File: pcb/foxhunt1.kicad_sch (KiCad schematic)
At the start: 0 parts

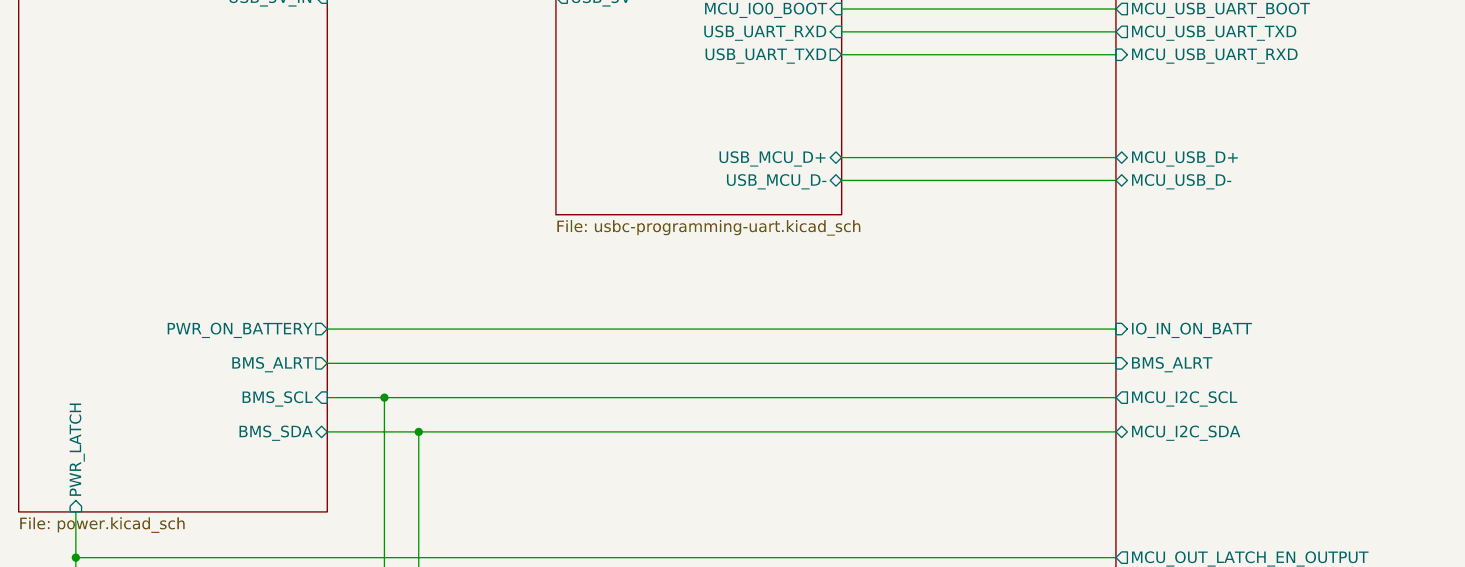
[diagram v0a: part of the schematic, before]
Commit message: Fix second mass-symbol-update reversion (recurred at same scale)
Same class of damage as the previous fix (commit 4ab9510) -- another
project-wide symbol resync reverted ~65 Datasheet fields and 5 Footprints
(Y2 crystal back to the wrong 5.0x3.2mm package again, U9/U12/U10/Y1
footprints back to non-stock equivalents) across all 7 schematic files.
Restored every field to its previously-verified value.

Also caught two real, independent bugs surfaced while re-checking (not
caused by this reversion, pre-existing): R32/R33/R43/R18 (10k YAGEO
RT0603BRD0710KL pull-ups, C95204) all had a mismatched Datasheet pointing
to a different resistor's PDF (RC0805FR-0710KL, wrong package family);
C36's Datasheet had drifted back to a different capacitor's PDF again
(same bug fixed once already this session).

ERC clean, same 14 pre-existing errors, no regressions.

Co-Authored-By: Claude Sonnet 5 <noreply@anthropic.com>
Claude-Session: https://claude.ai/code/session_01LhLkuH6sQ5GbUZ61bG7p2h
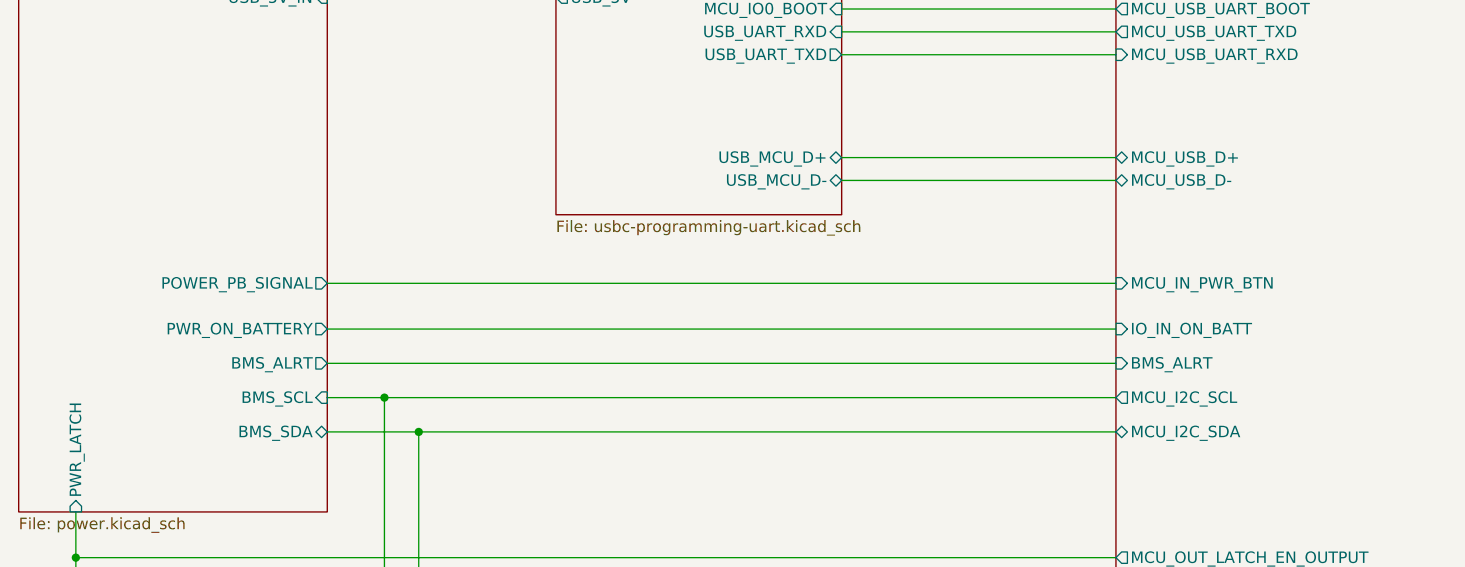
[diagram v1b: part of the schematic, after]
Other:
- sheet Power ports: added POWER_PB_SIGNAL; removed none
- sheet mcu-esp32 ports: added MCU_IN_PWR_BTN; removed none
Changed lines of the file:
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@@
+	(wire
+		(pts
+			(xy 78.74 74.93) (xy 166.37 74.93)
+		)
+		(stroke
+			(width 0)
+			(type default)
+		)
+	)
 	(wire
 		(pts
@@
 			)
 		)
+		(pin "POWER_PB_SIGNAL" output
+			(at 78.74 74.93 0)
+			(effects
+				(font
+					(size 1.27 1.27)
+				)
+				(justify right)
+			)
+		)
 		(instances
 			(project "foxhunt1"
@@
 			(effects
 				(font
+					(size 1.27 1.27)
+				)
+				(justify left)
+			)
+		)
+		(pin "MCU_IN_PWR_BTN" input
+			(at 166.37 74.93 180)
+			(effects
+				(font

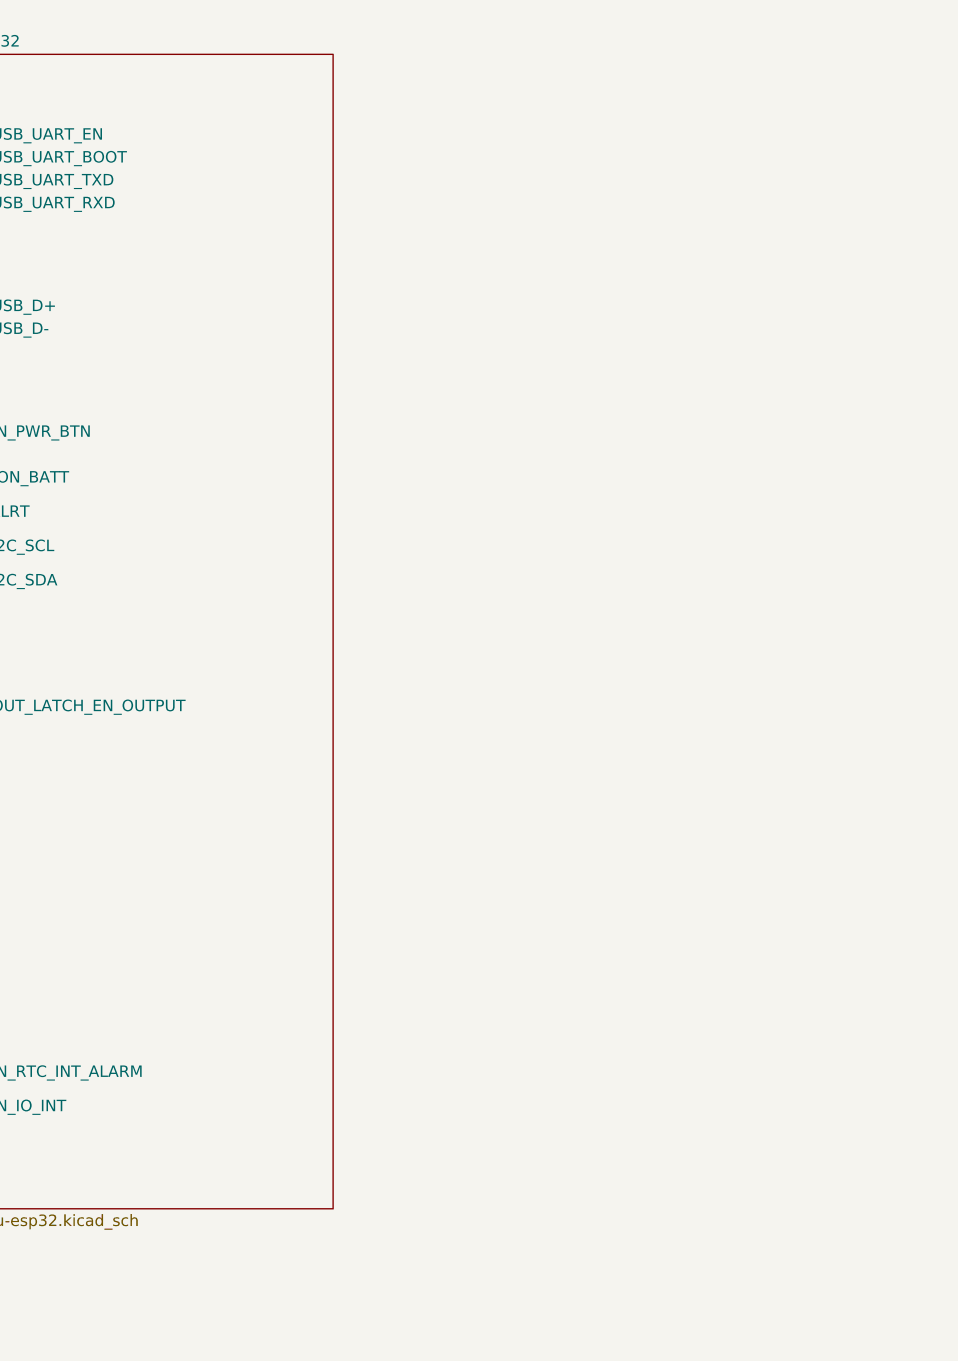
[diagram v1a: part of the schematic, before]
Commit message: Add I2S audio (PCM5102A) and GPS (MAX-M10S) schematic sheets
Audio: PCM5102A DAC with charge-pump network, per-channel output
filters, OUTL mic-level attenuator (divider + DC-block cap) for
SA818S/HT feed, OUTR spare-channel JST breakout, XSMT wired to the
board's last spare GPIO (GPIO3) for MCU-controlled muting.

GPS: MAX-M10S module, UART+PPS to ESP32-S3 (IO17/IO18/IO5), SMA RF
input with active-antenna bias-tee (bench through-hole SMA connector
for now, SMD swap planned), CR2032 holder placed (backup diode-OR
network not yet wired in).

Co-Authored-By: Claude Sonnet 5 <noreply@anthropic.com>
Claude-Session: https://claude.ai/code/session_01LhLkuH6sQ5GbUZ61bG7p2h
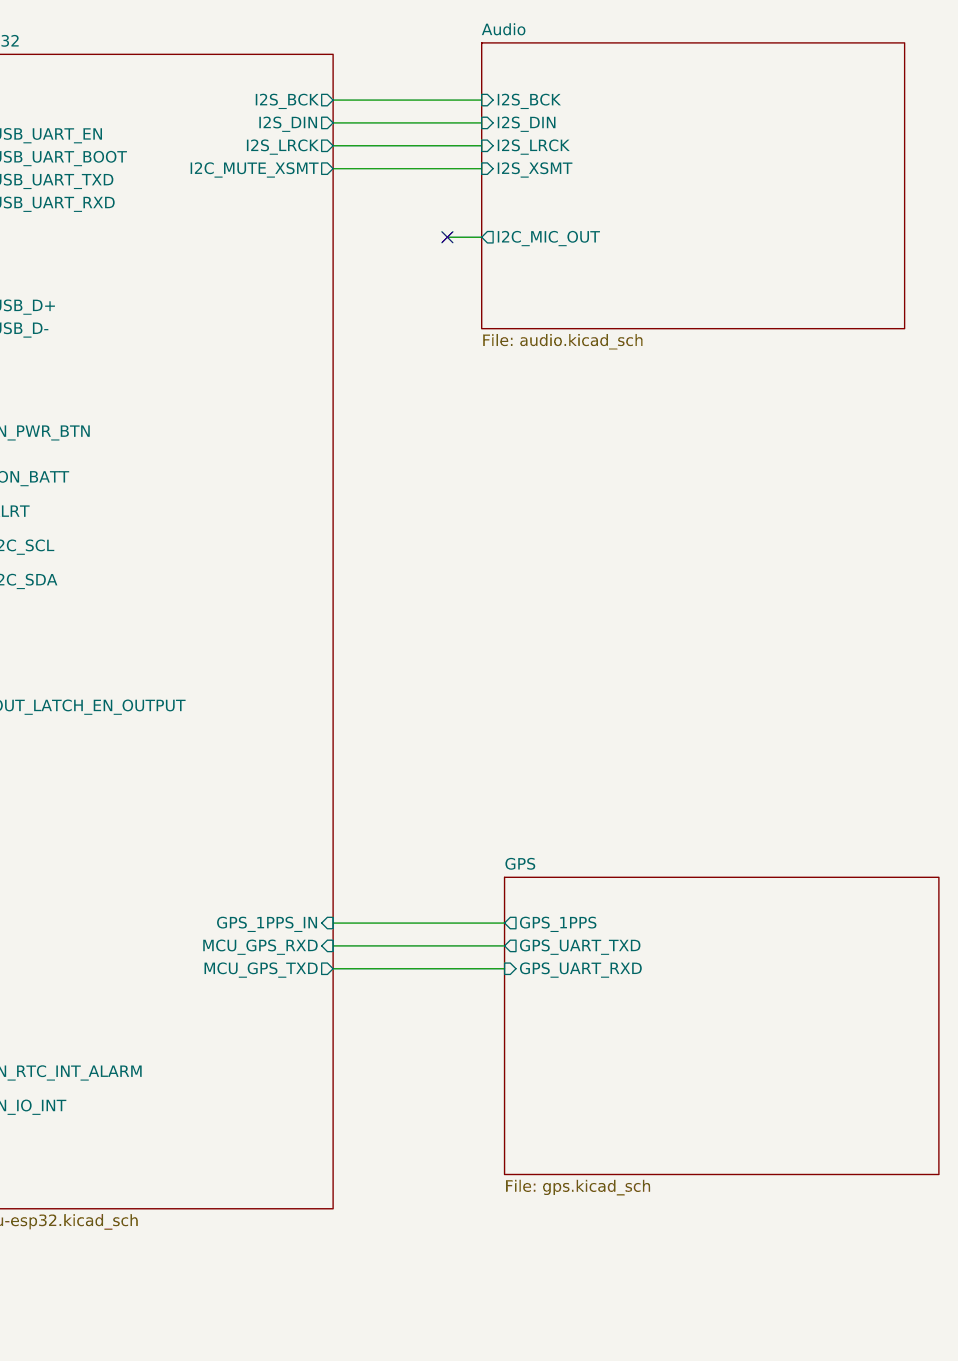
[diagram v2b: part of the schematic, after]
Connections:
- no-connect marks 0 -> 1
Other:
- added sheet Audio (audio.kicad_sch)
- added sheet GPS (gps.kicad_sch)
- sheet mcu-esp32 ports: added GPS_1PPS_IN, I2C_MUTE_XSMT, I2S_BCK, I2S_DIN, I2S_LRCK, MCU_GPS_RXD, MCU_GPS_TXD; removed none

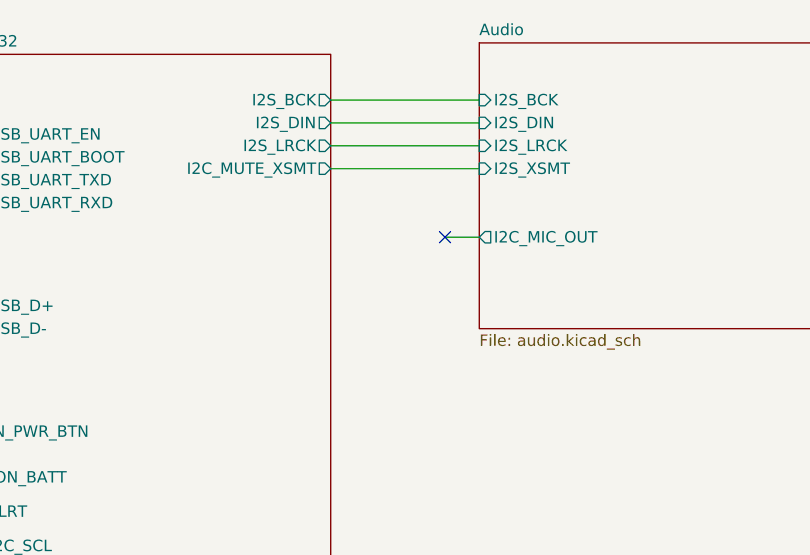
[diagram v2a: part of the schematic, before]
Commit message: Add external HT jack (J11) and PTT keying FET (Q10)
J11 (CUI/Same Sky SJ2-3593D-SMT-TR, switched TRS): tip and ring
switches auto-disconnect the onboard SA818S audio/PTT feeds the
instant something is plugged in. Q10 (BSS138) keys the shared PTT
node from GPIO16, with R53 (10k) pull-up holding it released by
default. Reviewed: T/TN and R/RN wiring both verified correct
against the jack's normalling behavior.

Co-Authored-By: Claude Sonnet 5 <noreply@anthropic.com>
Claude-Session: https://claude.ai/code/session_01LhLkuH6sQ5GbUZ61bG7p2h
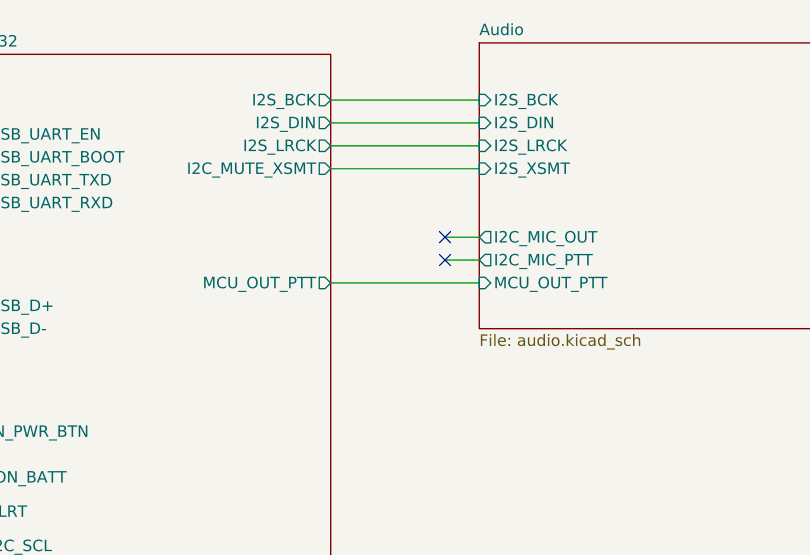
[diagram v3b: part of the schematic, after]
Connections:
- no-connect marks 1 -> 2
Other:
- sheet Audio ports: added I2C_MIC_PTT, MCU_OUT_PTT; removed none
- sheet mcu-esp32 ports: added MCU_OUT_PTT; removed none
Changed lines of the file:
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@@
 		(at 223.52 53.34)
 	)
+	(no_connect
+		(at 223.52 55.88)
+	)
 	(wire
 		(pts
@@
 	(wire
 		(pts
+			(xy 223.52 55.88) (xy 227.33 55.88)
+		)
+		(stroke
+			(width 0)
+			(type default)
+		)
+	)
+	(wire
+		(pts
 			(xy 135.89 46.99) (xy 166.37 46.99)
 		)
@@
 		(pts
 			(xy 135.89 41.91) (xy 166.37 41.91)
+		)
+		(stroke
+			(width 0)
+			(type default)
+		)
+	)
+	(wire
+		(pts
+			(xy 210.82 58.42) (xy 227.33 58.42)
 		)
 		(stroke
@@
 			)
 		)
+		(pin "MCU_OUT_PTT" output
+			(at 210.82 58.42 0)
+			(effects
+				(font
+					(size 1.27 1.27)
+				)
+				(justify right)
+			)
+		)
 		(instances
 			(project "foxhunt1"
@@
 			(effects
 				(font
+					(size 1.27 1.27)
+				)
+				(justify left)
+			)
+		)
+		(pin "I2C_MIC_PTT" output
+			(at 227.33 55.88 180)
+			(effects
+				(font
+					(size 1.27 1.27)
+				)
+				(justify left)
+			)
+		)
+		(pin "MCU_OUT_PTT" input
+			(at 227.33 58.42 180)
+			(effects
+				(font
